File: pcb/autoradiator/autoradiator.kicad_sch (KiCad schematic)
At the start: 12 parts, among them J1 Barrel_Jack_MountingPin, J2 Conn_01x02_Female, U1 ChineseDCDCBoard, U2 WeMos_D1_mini, U3 DRV8870DDA

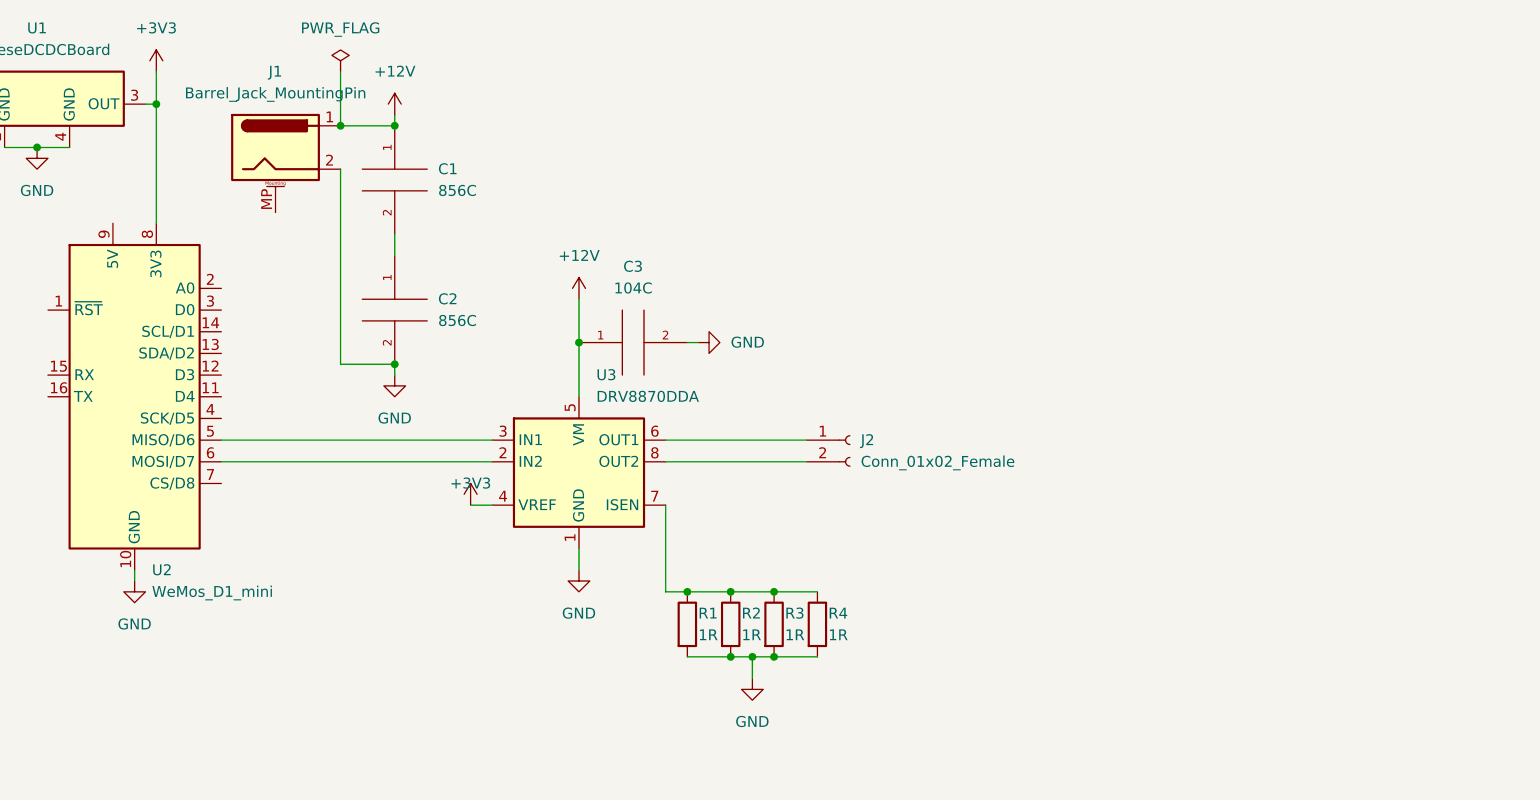
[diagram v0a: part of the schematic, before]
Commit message: Adjusted resistor values to limit current properly for test hardware and updated configuration to use more appropriate controls in homeassistant
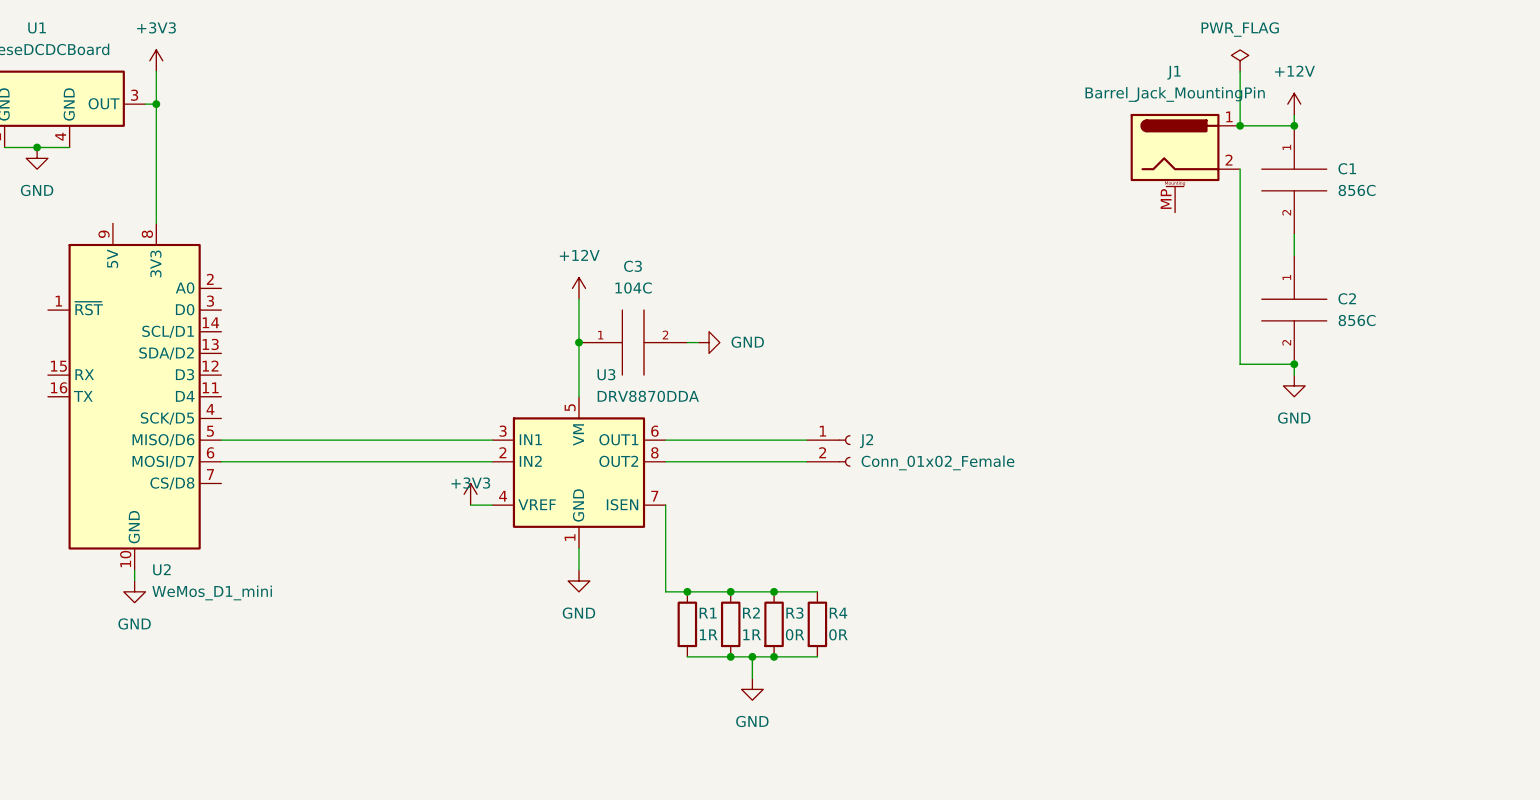
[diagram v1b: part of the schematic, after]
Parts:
- R3, R4: value 1R -> 0R
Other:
- moved on the sheet: C1, C2, J1
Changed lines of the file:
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@@
 (kicad_sch (version 20211123) (generator eeschema)
   (paper "A4")
-  (junction (at 93.98 57.15) (diameter 0) (color 0 0 0 0)
+  (junction (at 199.39 57.15) (diameter 0) (color 0 0 0 0)
   )
   (junction (at 128.27 83.82) (diameter 0) (color 0 0 0 0)
@@
   (junction (at 133.35 91.44) (diameter 0) (color 0 0 0 0)
   )
-  (junction (at 93.98 29.21) (diameter 0) (color 0 0 0 0)
-  )
-  (junction (at 87.63 29.21) (diameter 0) (color 0 0 0 0)
-  )
-  (wire (pts (xy 93.98 57.15) (xy 93.98 58.42))
+  (junction (at 199.39 29.21) (diameter 0) (color 0 0 0 0)
+  )
+  (junction (at 193.04 29.21) (diameter 0) (color 0 0 0 0)
+  )
+  (wire (pts (xy 199.39 57.15) (xy 199.39 58.42))
     (stroke (width 0) (type default) (color 0 0 0 0))
   )
@@
     (stroke (width 0) (type default) (color 0 0 0 0))
   )
-  (wire (pts (xy 87.63 22.86) (xy 87.63 29.21))
-    (stroke (width 0) (type default) (color 0 0 0 0))
-  )
-  (wire (pts (xy 93.98 27.94) (xy 93.98 29.21))
+  (wire (pts (xy 193.04 22.86) (xy 193.04 29.21))
+    (stroke (width 0) (type default) (color 0 0 0 0))
+  )
+  (wire (pts (xy 199.39 27.94) (xy 199.39 29.21))
     (stroke (width 0) (type default) (color 0 0 0 0))
   )
@@
     (stroke (width 0) (type default) (color 0 0 0 0))
   )
-  (wire (pts (xy 93.98 41.91) (xy 93.98 44.45))
-    (stroke (width 0) (type default) (color 0 0 0 0))
-  )
-  (wire (pts (xy 87.63 57.15) (xy 93.98 57.15))
-    (stroke (width 0) (type default) (color 0 0 0 0))
-  )
-  (wire (pts (xy 87.63 29.21) (xy 93.98 29.21))
+  (wire (pts (xy 199.39 41.91) (xy 199.39 44.45))
+    (stroke (width 0) (type default) (color 0 0 0 0))
+  )
+  (wire (pts (xy 193.04 57.15) (xy 199.39 57.15))
+    (stroke (width 0) (type default) (color 0 0 0 0))
+  )
+  (wire (pts (xy 193.04 29.21) (xy 199.39 29.21))
     (stroke (width 0) (type default) (color 0 0 0 0))
   )
@@
     (stroke (width 0) (type default) (color 0 0 0 0))
   )
-  (wire (pts (xy 87.63 34.29) (xy 87.63 57.15))
+  (wire (pts (xy 193.04 34.29) (xy 193.04 57.15))
     (stroke (width 0) (type default) (color 0 0 0 0))
   )
@@
     (pin "1")
   )
-  (symbol (lib_id "pspice:C") (at 93.98 50.8 0) (unit 1)
-    (in_bom yes) (on_board yes) (fields_autoplaced)
-    (property "Reference" "C2" (id 0) (at 99.06 49.5299 0)
-      (effects (font (size 1.27 1.27)) (justify left))
-    )
-    (property "Value" "856C" (id 1) (at 99.06 52.0699 0)
-      (effects (font (size 1.27 1.27)) (justify left))
-    )
-    (property "Footprint" "Capacitor_SMD:C_1206_3216Metric_Pad1.33x1.80mm_HandSolder" (id 2) (at 93.98 50.8 0)
-      (effects (font (size 1.27 1.27)) hide)
-    )
-    (property "Datasheet" "~" (id 3) (at 93.98 50.8 0)
+  (symbol (lib_id "pspice:C") (at 199.39 50.8 0) (unit 1)
+    (in_bom yes) (on_board yes) (fields_autoplaced)
+    (property "Reference" "C2" (id 0) (at 204.47 49.5299 0)
+      (effects (font (size 1.27 1.27)) (justify left))
+    )
+    (property "Value" "856C" (id 1) (at 204.47 52.0699 0)
+      (effects (font (size 1.27 1.27)) (justify left))
+    )
+    (property "Footprint" "Capacitor_SMD:C_1206_3216Metric_Pad1.33x1.80mm_HandSolder" (id 2) (at 199.39 50.8 0)
+      (effects (font (size 1.27 1.27)) hide)
+    )
+    (property "Datasheet" "~" (id 3) (at 199.39 50.8 0)
       (effects (font (size 1.27 1.27)) hide)
     )
@@
     (pin "9")
   )
-  (symbol (lib_id "power:+12V") (at 93.98 27.94 0) (unit 1)
-    (in_bom yes) (on_board yes) (fields_autoplaced)
-    (property "Reference" "#PWR05" (id 0) (at 93.98 31.75 0)
-      (effects (font (size 1.27 1.27)) hide)
-    )
-    (property "Value" "+12V" (id 1) (at 93.98 22.86 0))
-    (property "Footprint" "" (id 2) (at 93.98 27.94 0)
-      (effects (font (size 1.27 1.27)) hide)
-    )
-    (property "Datasheet" "" (id 3) (at 93.98 27.94 0)
+  (symbol (lib_id "power:+12V") (at 199.39 27.94 0) (unit 1)
+    (in_bom yes) (on_board yes) (fields_autoplaced)
+    (property "Reference" "#PWR05" (id 0) (at 199.39 31.75 0)
+      (effects (font (size 1.27 1.27)) hide)
+    )
+    (property "Value" "+12V" (id 1) (at 199.39 22.86 0))
+    (property "Footprint" "" (id 2) (at 199.39 27.94 0)
+      (effects (font (size 1.27 1.27)) hide)
+    )
+    (property "Datasheet" "" (id 3) (at 199.39 27.94 0)
       (effects (font (size 1.27 1.27)) hide)
     )
@@
     (pin "1")
   )
-  (symbol (lib_id "power:GND") (at 93.98 58.42 0) (unit 1)
-    (in_bom yes) (on_board yes) (fields_autoplaced)
-    (property "Reference" "#PWR06" (id 0) (at 93.98 64.77 0)
-      (effects (font (size 1.27 1.27)) hide)
-    )
-    (property "Value" "GND" (id 1) (at 93.98 63.5 0))
-    (property "Footprint" "" (id 2) (at 93.98 58.42 0)
-      (effects (font (size 1.27 1.27)) hide)
-    )
-    (property "Datasheet" "" (id 3) (at 93.98 58.42 0)
-      (effects (font (size 1.27 1.27)) hide)
-    )
-    (pin "1")
-  )
-  (symbol (lib_id "power:PWR_FLAG") (at 87.63 22.86 0) (unit 1)
-    (in_bom yes) (on_board yes) (fields_autoplaced)
-    (property "Reference" "#FLG0101" (id 0) (at 87.63 20.955 0)
-      (effects (font (size 1.27 1.27)) hide)
-    )
-    (property "Value" "PWR_FLAG" (id 1) (at 87.63 17.78 0))
-    (property "Footprint" "" (id 2) (at 87.63 22.86 0)
-      (effects (font (size 1.27 1.27)) hide)
-    )
-    (property "Datasheet" "~" (id 3) (at 87.63 22.86 0)
+  (symbol (lib_id "power:GND") (at 199.39 58.42 0) (unit 1)
+    (in_bom yes) (on_board yes) (fields_autoplaced)
+    (property "Reference" "#PWR06" (id 0) (at 199.39 64.77 0)
+      (effects (font (size 1.27 1.27)) hide)
+    )
+    (property "Value" "GND" (id 1) (at 199.39 63.5 0))
+    (property "Footprint" "" (id 2) (at 199.39 58.42 0)
+      (effects (font (size 1.27 1.27)) hide)
+    )
+    (property "Datasheet" "" (id 3) (at 199.39 58.42 0)
+      (effects (font (size 1.27 1.27)) hide)
+    )
+    (pin "1")
+  )
+  (symbol (lib_id "power:PWR_FLAG") (at 193.04 22.86 0) (unit 1)
+    (in_bom yes) (on_board yes) (fields_autoplaced)
+    (property "Reference" "#FLG0101" (id 0) (at 193.04 20.955 0)
+      (effects (font (size 1.27 1.27)) hide)
+    )
+    (property "Value" "PWR_FLAG" (id 1) (at 193.04 17.78 0))
+    (property "Footprint" "" (id 2) (at 193.04 22.86 0)
+      (effects (font (size 1.27 1.27)) hide)
+    )
+    (property "Datasheet" "~" (id 3) (at 193.04 22.86 0)
       (effects (font (size 1.27 1.27)) hide)
     )
@@
       (effects (font (size 1.27 1.27)) (justify left))
     )
-    (property "Value" "1R" (id 1) (at 144.78 88.9 0)
+    (property "Value" "0R" (id 1) (at 144.78 88.9 0)
       (effects (font (size 1.27 1.27)) (justify left))
     )
@@
       (effects (font (size 1.27 1.27)) (justify left))
     )
-    (property "Value" "1R" (id 1) (at 139.7 88.9 0)
+    (property "Value" "0R" (id 1) (at 139.7 88.9 0)
       (effects (font (size 1.27 1.27)) (justify left))
     )
@@
     (pin "4")
   )
-  (symbol (lib_id "pspice:C") (at 93.98 35.56 0) (unit 1)
-    (in_bom yes) (on_board yes) (fields_autoplaced)
-    (property "Reference" "C1" (id 0) (at 99.06 34.2899 0)
-      (effects (font (size 1.27 1.27)) (justify left))
-    )
-    (property "Value" "856C" (id 1) (at 99.06 36.8299 0)
-      (effects (font (size 1.27 1.27)) (justify left))
-    )
-    (property "Footprint" "Capacitor_SMD:C_1206_3216Metric_Pad1.33x1.80mm_HandSolder" (id 2) (at 93.98 35.56 0)
-      (effects (font (size 1.27 1.27)) hide)
-    )
-    (property "Datasheet" "~" (id 3) (at 93.98 35.56 0)
+  (symbol (lib_id "pspice:C") (at 199.39 35.56 0) (unit 1)
+    (in_bom yes) (on_board yes) (fields_autoplaced)
+    (property "Reference" "C1" (id 0) (at 204.47 34.2899 0)
+      (effects (font (size 1.27 1.27)) (justify left))
+    )
+    (property "Value" "856C" (id 1) (at 204.47 36.8299 0)
+      (effects (font (size 1.27 1.27)) (justify left))
+    )
+    (property "Footprint" "Capacitor_SMD:C_1206_3216Metric_Pad1.33x1.80mm_HandSolder" (id 2) (at 199.39 35.56 0)
+      (effects (font (size 1.27 1.27)) hide)
+    )
+    (property "Datasheet" "~" (id 3) (at 199.39 35.56 0)
       (effects (font (size 1.27 1.27)) hide)
     )
@@
     (pin "1")
   )
-  (symbol (lib_id "Connector:Barrel_Jack_MountingPin") (at 80.01 31.75 0) (unit 1)
-    (in_bom yes) (on_board yes) (fields_autoplaced)
-    (property "Reference" "J1" (id 0) (at 80.01 22.86 0))
-    (property "Value" "Barrel_Jack_MountingPin" (id 1) (at 80.01 25.4 0))
-    (property "Footprint" "Connector_BarrelJack:BarrelJack_Wuerth_6941xx301002" (id 2) (at 81.28 32.766 0)
-      (effects (font (size 1.27 1.27)) hide)
-    )
-    (property "Datasheet" "~" (id 3) (at 81.28 32.766 0)
+  (symbol (lib_id "Connector:Barrel_Jack_MountingPin") (at 185.42 31.75 0) (unit 1)
+    (in_bom yes) (on_board yes) (fields_autoplaced)
+    (property "Reference" "J1" (id 0) (at 185.42 22.86 0))
+    (property "Value" "Barrel_Jack_MountingPin" (id 1) (at 185.42 25.4 0))
+    (property "Footprint" "Connector_BarrelJack:BarrelJack_Wuerth_6941xx301002" (id 2) (at 186.69 32.766 0)
+      (effects (font (size 1.27 1.27)) hide)
+    )
+    (property "Datasheet" "~" (id 3) (at 186.69 32.766 0)
       (effects (font (size 1.27 1.27)) hide)
     )
@@
     )
     (path "/6b75a637-4290-458e-9ca9-7a947f5ae499"
-      (reference "R3") (unit 1) (value "1R") (footprint "Resistor_SMD:R_1206_3216Metric_Pad1.30x1.75mm_HandSolder")
+      (reference "R3") (unit 1) (value "0R") (footprint "Resistor_SMD:R_1206_3216Metric_Pad1.30x1.75mm_HandSolder")
     )
     (path "/620e207a-b9e2-4c26-9cff-8d1c6e6f6803"
-      (reference "R4") (unit 1) (value "1R") (footprint "Resistor_SMD:R_1206_3216Metric_Pad1.30x1.75mm_HandSolder")
+      (reference "R4") (unit 1) (value "0R") (footprint "Resistor_SMD:R_1206_3216Metric_Pad1.30x1.75mm_HandSolder")
     )
     (path "/92d38b6e-10bb-4476-90f2-2e4d27e77bb1"

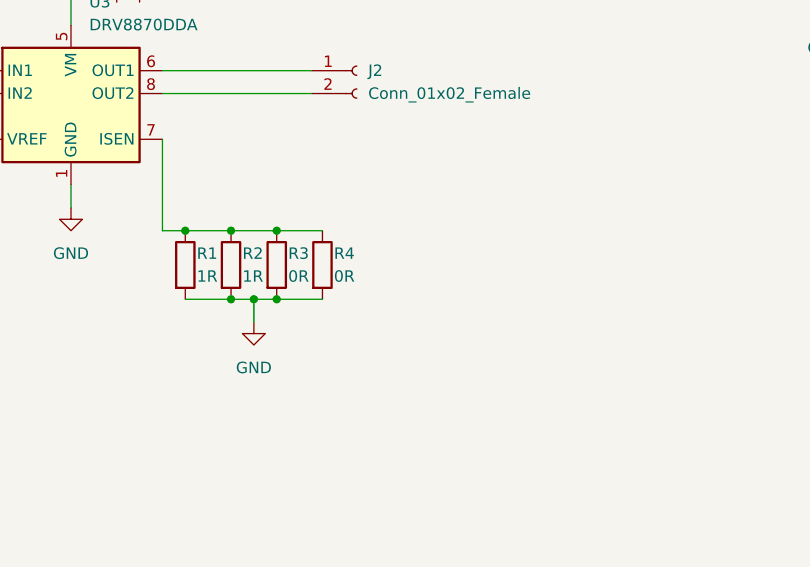
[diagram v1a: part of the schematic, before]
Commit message: Updated PCB to mark some resistors as not populated
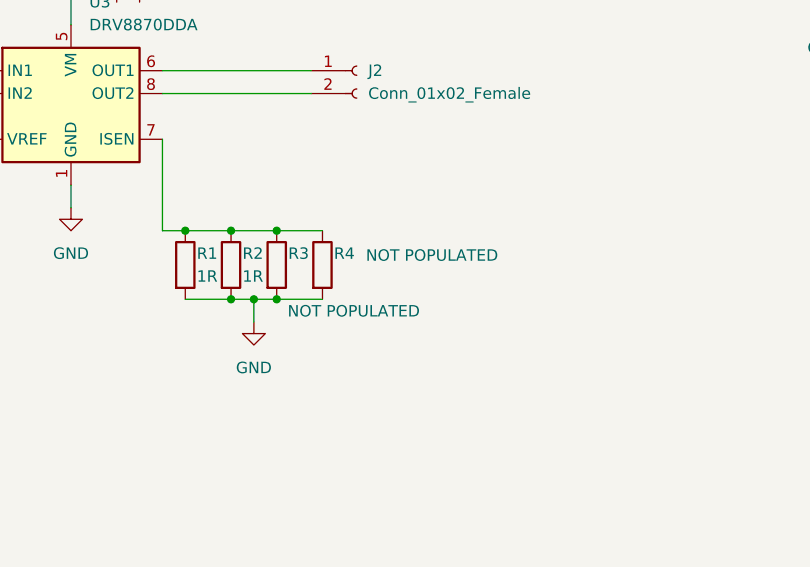
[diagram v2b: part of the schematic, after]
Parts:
- R3, R4: value 0R -> NOT POPULATED
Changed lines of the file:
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@@
       (effects (font (size 1.27 1.27)) (justify left))
     )
-    (property "Value" "0R" (id 1) (at 144.78 88.9 0)
+    (property "Value" "NOT POPULATED" (id 1) (at 148.3305 86.5695 0)
       (effects (font (size 1.27 1.27)) (justify left))
     )
@@
       (effects (font (size 1.27 1.27)) (justify left))
     )
-    (property "Value" "0R" (id 1) (at 139.7 88.9 0)
+    (property "Value" "NOT POPULATED" (id 1) (at 139.6319 92.764 0)
       (effects (font (size 1.27 1.27)) (justify left))
     )
@@
     )
     (path "/6b75a637-4290-458e-9ca9-7a947f5ae499"
-      (reference "R3") (unit 1) (value "0R") (footprint "Resistor_SMD:R_1206_3216Metric_Pad1.30x1.75mm_HandSolder")
+      (reference "R3") (unit 1) (value "NOT POPULATED") (footprint "Resistor_SMD:R_1206_3216Metric_Pad1.30x1.75mm_HandSolder")
     )
     (path "/620e207a-b9e2-4c26-9cff-8d1c6e6f6803"
-      (reference "R4") (unit 1) (value "0R") (footprint "Resistor_SMD:R_1206_3216Metric_Pad1.30x1.75mm_HandSolder")
+      (reference "R4") (unit 1) (value "NOT POPULATED") (footprint "Resistor_SMD:R_1206_3216Metric_Pad1.30x1.75mm_HandSolder")
     )
     (path "/92d38b6e-10bb-4476-90f2-2e4d27e77bb1"
